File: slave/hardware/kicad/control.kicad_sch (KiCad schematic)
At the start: 29 parts, among them IC9 STM32G431C8T6TR, SW1 SW_Push, SW2 SW_Push, Y1 8Mhz

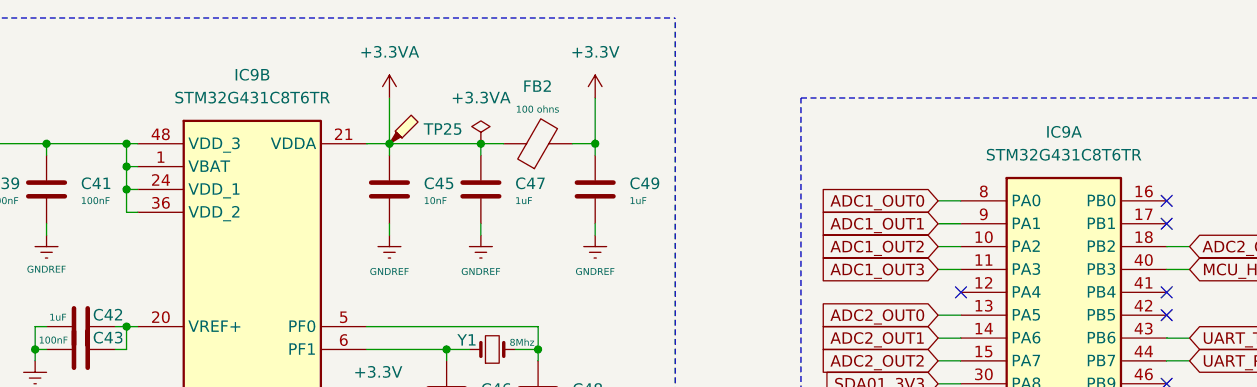
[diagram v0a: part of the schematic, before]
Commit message: fix(HW): resolve KiCad ERC warnings
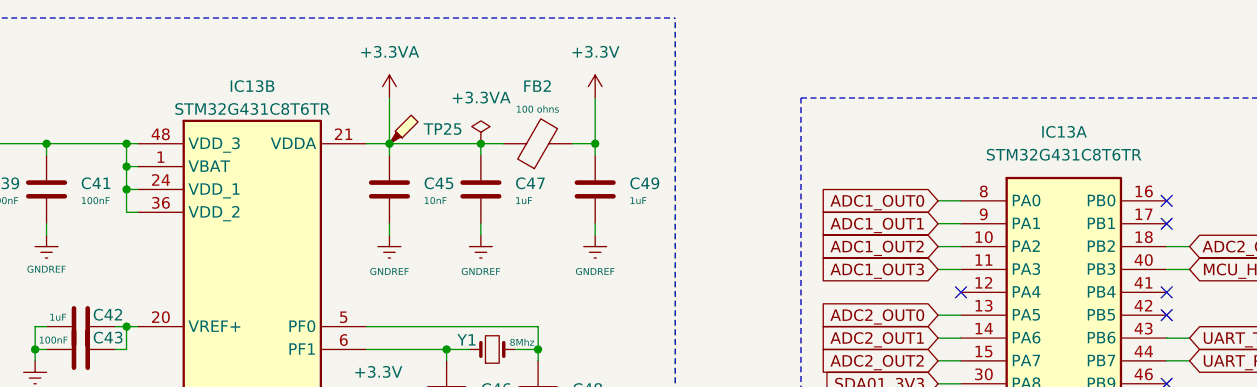
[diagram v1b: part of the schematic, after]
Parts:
- removed IC9: STM32G431C8T6TR, Datalogger:QFP50P900X900X160-48N, symbol Datalogger Slave:STM32G431C8T6TR_SPLIT
- added IC13: STM32G431C8T6TR, Datalogger:QFP50P900X900X160-48N, symbol Datalogger:STM32G431C8T6TR_SPLIT
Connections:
- net +3.3V: now also IC13.1 (VBAT), IC13.24 (VDD_1), IC13.36 (VDD_2), IC13.48 (VDD_3)
- net +3.3VA: now also IC13.21 (VDDA)
- net ADC1_OUT0: now also IC13.8 (PA0)
- net ADC1_OUT1: now also IC13.9 (PA1)
- net ADC1_OUT2: now also IC13.10 (PA2)
- net ADC1_OUT3: now also IC13.11 (PA3)
- net ADC2_OUT0: now also IC13.13 (PA5)
- net ADC2_OUT1: now also IC13.14 (PA6)
- net ADC2_OUT2: now also IC13.15 (PA7)
- net ADC2_OUT3: now also IC13.18 (PB2)
- net BOOT0: now also IC13.45 (BOOT)
- net CAN_RX: now also IC13.33 (PA11)
- net CAN_STATUS: now also IC13.3 (PC14)
- net CAN_TX: now also IC13.34 (PA12)
- net GNDREF: now also IC13.19 (VSSA), IC13.23 (VSS_1), IC13.35 (VSS_2), IC13.47 (VSS_3)
- net HEARTBEAT: now also IC13.4 (PC15)
- net MCU_HS_01: now also IC13.40 (PB3)
- net MCU_HS_02: now also IC13.39 (PA15)
- net MCU_LS_01: now also IC13.25 (PB11)
- net MCU_LS_02: now also IC13.26 (PB12)
- net MCU_LS_03: now also IC13.27 (PB13)
- net MCU_LS_04: now also IC13.28 (PB14)
- net NRST: now also IC13.7 (PG10)
- net SCL01_3V3: now also IC13.31 (PA9)
- net SDA01_3V3: now also IC13.30 (PA8)
- net TRIGGER: now also IC13.2 (PC13)
- net UART_RX: now also IC13.44 (PB7)
- net UART_TX: now also IC13.43 (PB6)
- net at C46.1, Y1.1: now also IC13.6 (PF1)
- net at C42.2, C43.2: now also IC13.20 (VREF+)
- net at C48.1, Y1.2: now also IC13.5 (PF0)

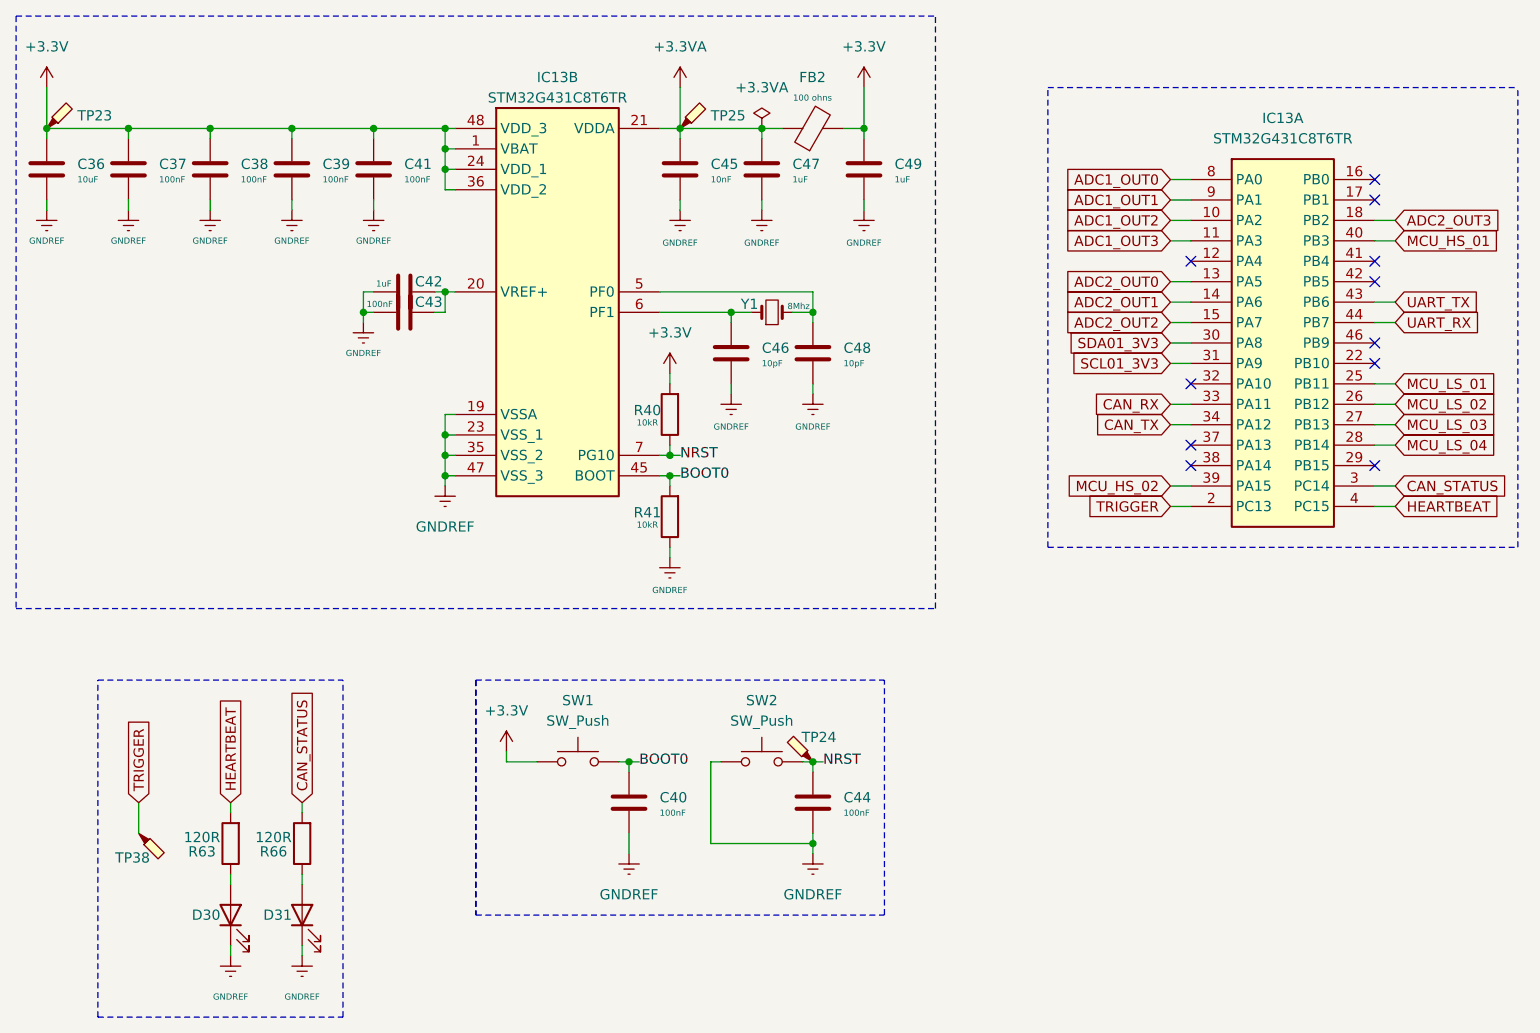
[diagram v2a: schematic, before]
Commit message: feat(HW): continue PCB layout and routing updates
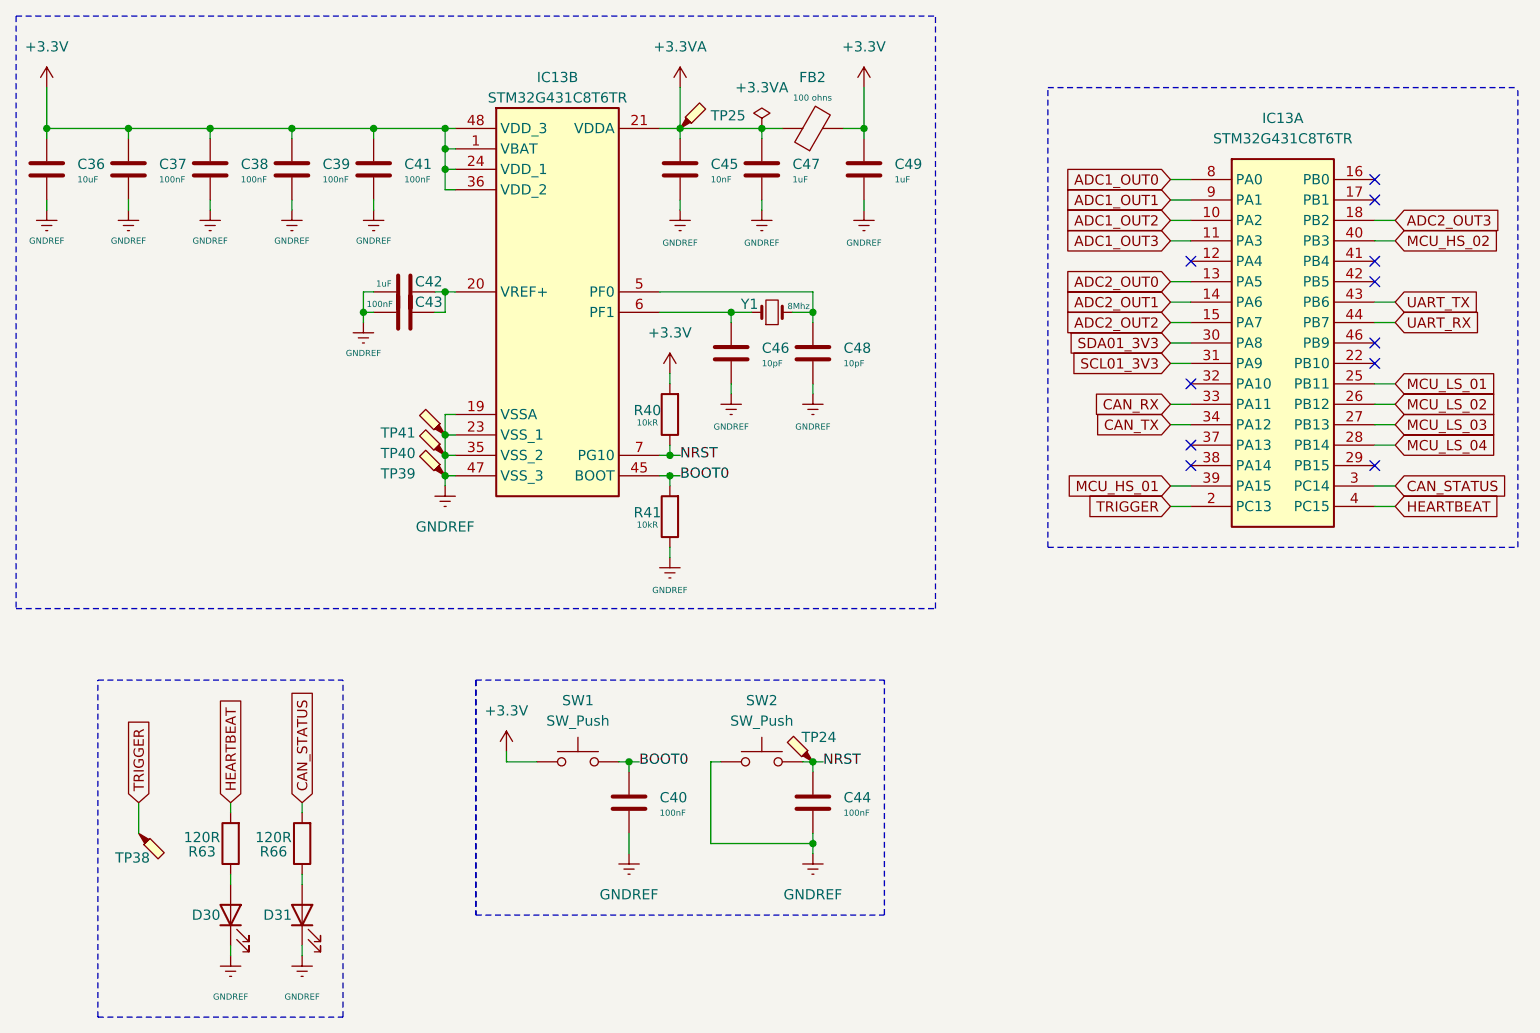
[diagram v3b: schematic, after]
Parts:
- removed TP23: (no value), TestPoint:TestPoint_Pad_2.0x2.0mm, symbol Connector:TestPoint_Probe
- added TP39, TP40, TP41: (no value), TestPoint:TestPoint_Bridge_Pitch2.0mm_Drill0.7mm, symbol Connector:TestPoint_Probe
- C36, C37, C38, C39, C40, C41, C42, C43, C44, C45, C46, C47, C48, C49, FB2: footprint Capacitor_SMD:C_0201_0603Metric -> Capacitor_SMD:C_0603_1608Metric
- D30, D31: footprint LED_SMD:LED_01005_0402Metric -> LED_SMD:LED_0805_2012Metric
- TP38: footprint TestPoint:TestPoint_Pad_2.0x2.0mm -> TestPoint:TestPoint_Bridge_Pitch2.0mm_Drill0.7mm
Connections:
- net GNDREF: now also TP39.1, TP40.1, TP41.1
- net MCU_HS_01: now also IC13.39 (PA15); no longer IC13.40 (PB3)
- net MCU_HS_02: now also IC13.40 (PB3); no longer IC13.39 (PA15)
